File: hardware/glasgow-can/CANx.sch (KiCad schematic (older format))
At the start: 14 parts, among them J7 Conn_01x02_Male, Q1 TLP240A, Q2 NX7002BKW, U1 TCAN1051

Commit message: tidy up schematics
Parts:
- removed J7: Conn_01x02_Male, Connector_PinHeader_2.54mm:PinHeader_1x02_P2.54mm_Vertical, symbol Connector:Conn_01x02_Male
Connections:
- net CANH: now also D1.2 (A2); no longer D1.1 (A1)
- net CANL: now also D1.1 (A1); no longer D1.2 (A2)
- net S renamed SILENT
- no-connect marks 0 -> 1
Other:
- note added: "R1 is 1206 / 125mW\nIn fault (bus shorted) it will see:\nV= 24v R= 120Ω P= 24²/120= 4.8W"
- note added: "Red: Vf=2.0v Vr=3.0v I=100uA R=30kΩ\nGreen: Vf=3.0v Vr=2.0v I=20uA R=100kΩ *\nBlue: Vf=3.0v Vr=2.0v I=100uA R=20kΩ\n\n* Green has far higher lumosity, so current is reduced."
- note added: "Red:\nGreen:\nBlue:"
- note added: "Silent Active\nCAN Tx\nCAN Rx"
- note added: "Status LED"
- note added: "Termination"
- note added: "V= 5v I= 7.5mA\nVf= 1.27v Vr= 3.73v\nR= 506Ω -> 510Ω"
- note removed: "I=200mA R=120Ohm P=4.8W"
- note removed: "Red: Vf=2.0v I=100uA Vr=3.0v R=30kOhm\nGreen: Vf=3.0v I=20uA Vr=2.0v R=100kOhm\nBlue: Vf=3.0v I=100uA Vr=2.0v R=20kOhm"
- note removed: "V = 5v Vf = 1.27v \nVr = 3.73v I = 7.5mA\nR = 506 Ohm -> 510 Ohm"
- moved on the sheet: C1, C2, D1, D2, Q1, Q2, R1, R2, R3, R4, R5, R6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

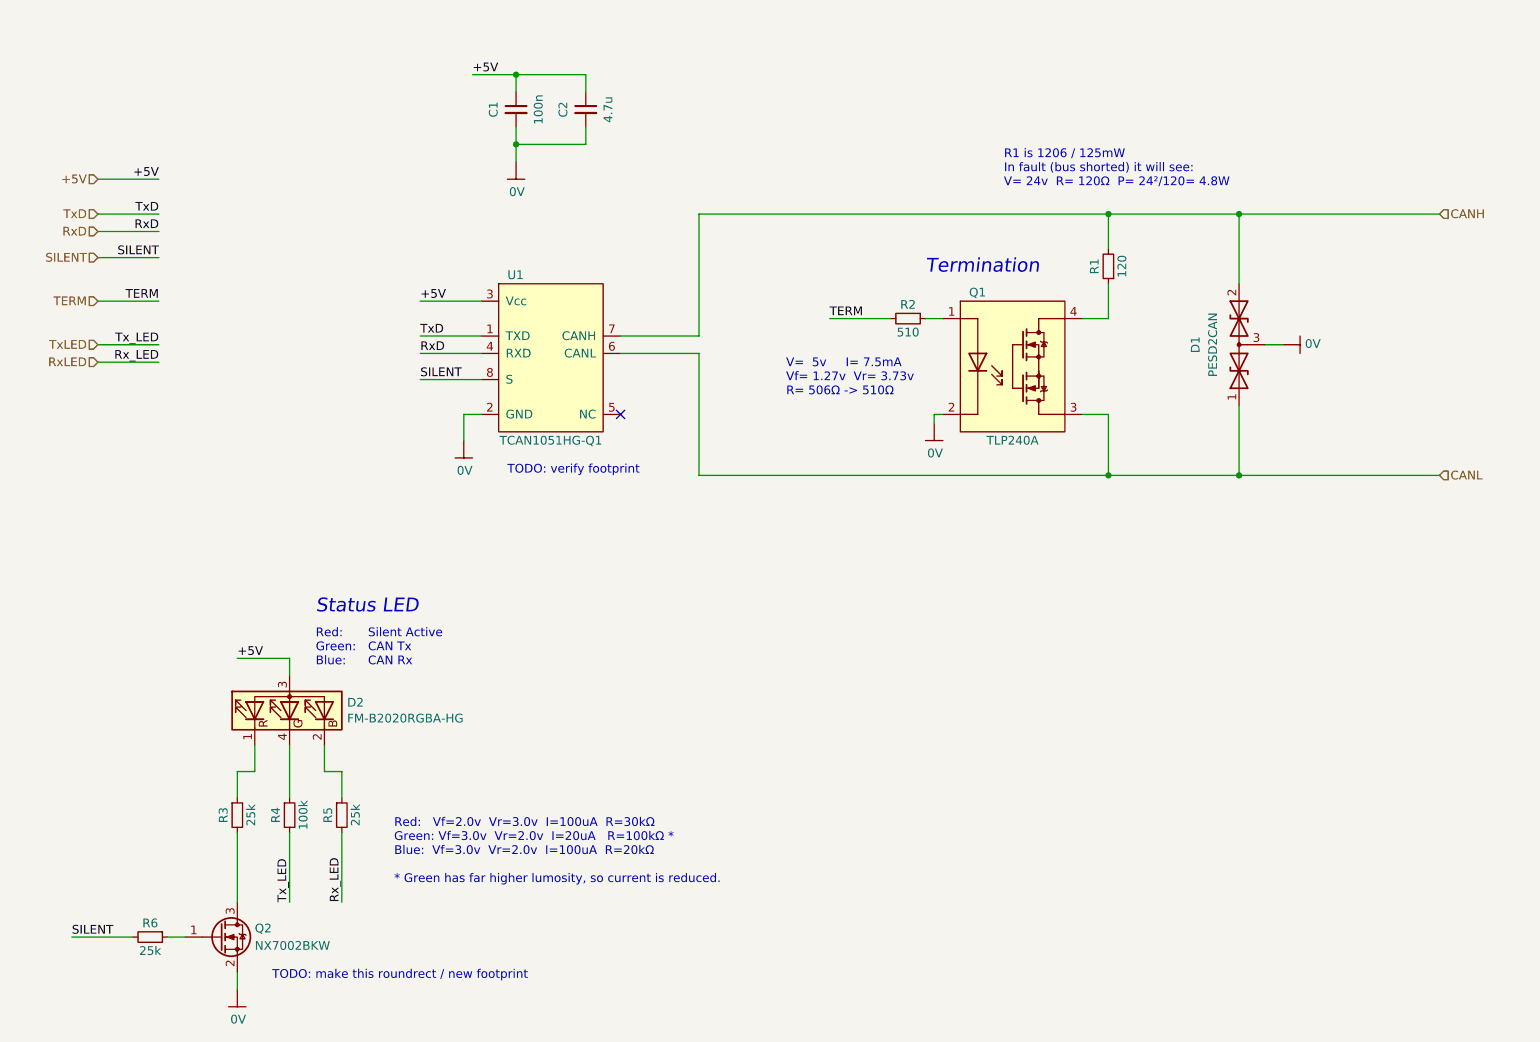
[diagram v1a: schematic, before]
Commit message: schematic revised according to discussion in #1, and layout mostly complete... some TODOs remain
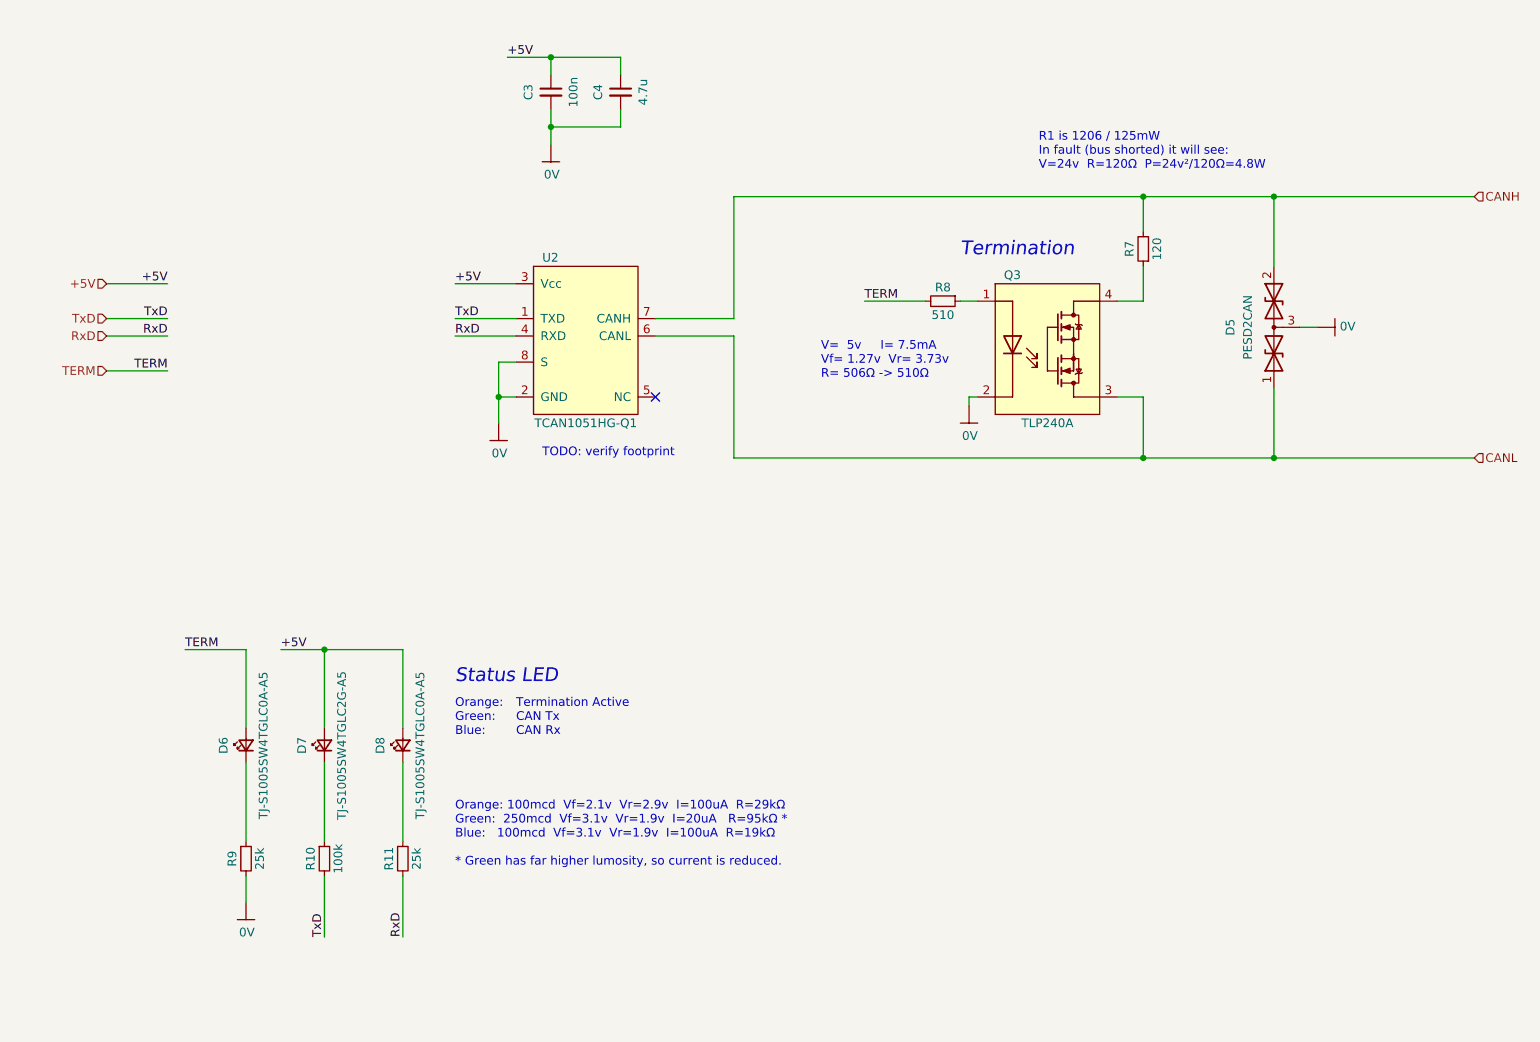
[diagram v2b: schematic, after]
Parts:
- removed D2: FM-B2020RGBA-HG, pkl_led:LED_TRI_2020, symbol Device:LED_RBAG
- removed Q2: NX7002BKW, Package_TO_SOT_SMD:SOT-323_SC-70, symbol Device:Q_NMOS_GSD
- removed R6: 25k, Resistor_SMD:R_0402_1005Metric, symbol Device:R_Small
- added D2, D4: TJ-S1005SW4TGLC0A-A5, LED_SMD:LED_0402_1005Metric_Pad0.77x0.64mm_HandSolder, symbol Device:LED_Small
- added D3: TJ-S1005SW4TGLC2G-A5, LED_SMD:LED_0402_1005Metric_Pad0.77x0.64mm_HandSolder, symbol Device:LED_Small
- Q1: MPN TLP240A -> TLP240A(TP1,F
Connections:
- net RxLED is gone; now on net RxD: R5.2
- net SILENT is gone; now on net 0V: U1.8 (S)
- net TxLED is gone; now on net TxD: R4.2
- net +5V: now also D3.2 (A), D4.2 (A)
- net 0V: now also R3.2
- net TERM: now also D2.2 (A)
- net at R4.1: now also D3.1 (K)
- net at R3.1: now also D2.1 (K)
- net at R5.1: now also D4.1 (K)
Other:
- note added: "Orange: 100mcd Vf=2.1v Vr=2.9v I=100uA R=29kΩ\nGreen: 250mcd Vf=3.1v Vr=1.9v I=20uA R=95kΩ *\nBlue: 100mcd Vf=3.1v Vr=1.9v I=100uA R=19kΩ\n\n* Green has far higher lumosity, so current is reduced."
- note added: "Orange:\nGreen:\nBlue:"
- note added: "R1 is 1206 / 125mW\nIn fault (bus shorted) it will see:\nV=24v R=120Ω P=24v²/120Ω=4.8W"
- note added: "Termination Active\nCAN Tx\nCAN Rx"
- note removed: "R1 is 1206 / 125mW\nIn fault (bus shorted) it will see:\nV= 24v R= 120Ω P= 24²/120= 4.8W"
- note removed: "Red: Vf=2.0v Vr=3.0v I=100uA R=30kΩ\nGreen: Vf=3.0v Vr=2.0v I=20uA R=100kΩ *\nBlue: Vf=3.0v Vr=2.0v I=100uA R=20kΩ\n\n* Green has far higher lumosity, so current is reduced."
- note removed: "Red:\nGreen:\nBlue:"
- note removed: "Silent Active\nCAN Tx\nCAN Rx"
- note removed: "TODO: make this roundrect / new footprint"
- moved on the sheet: C3, C4, D5, Q3, R7, R8, U2

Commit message: fix DE-9 footprint, spruce up schematic and layout
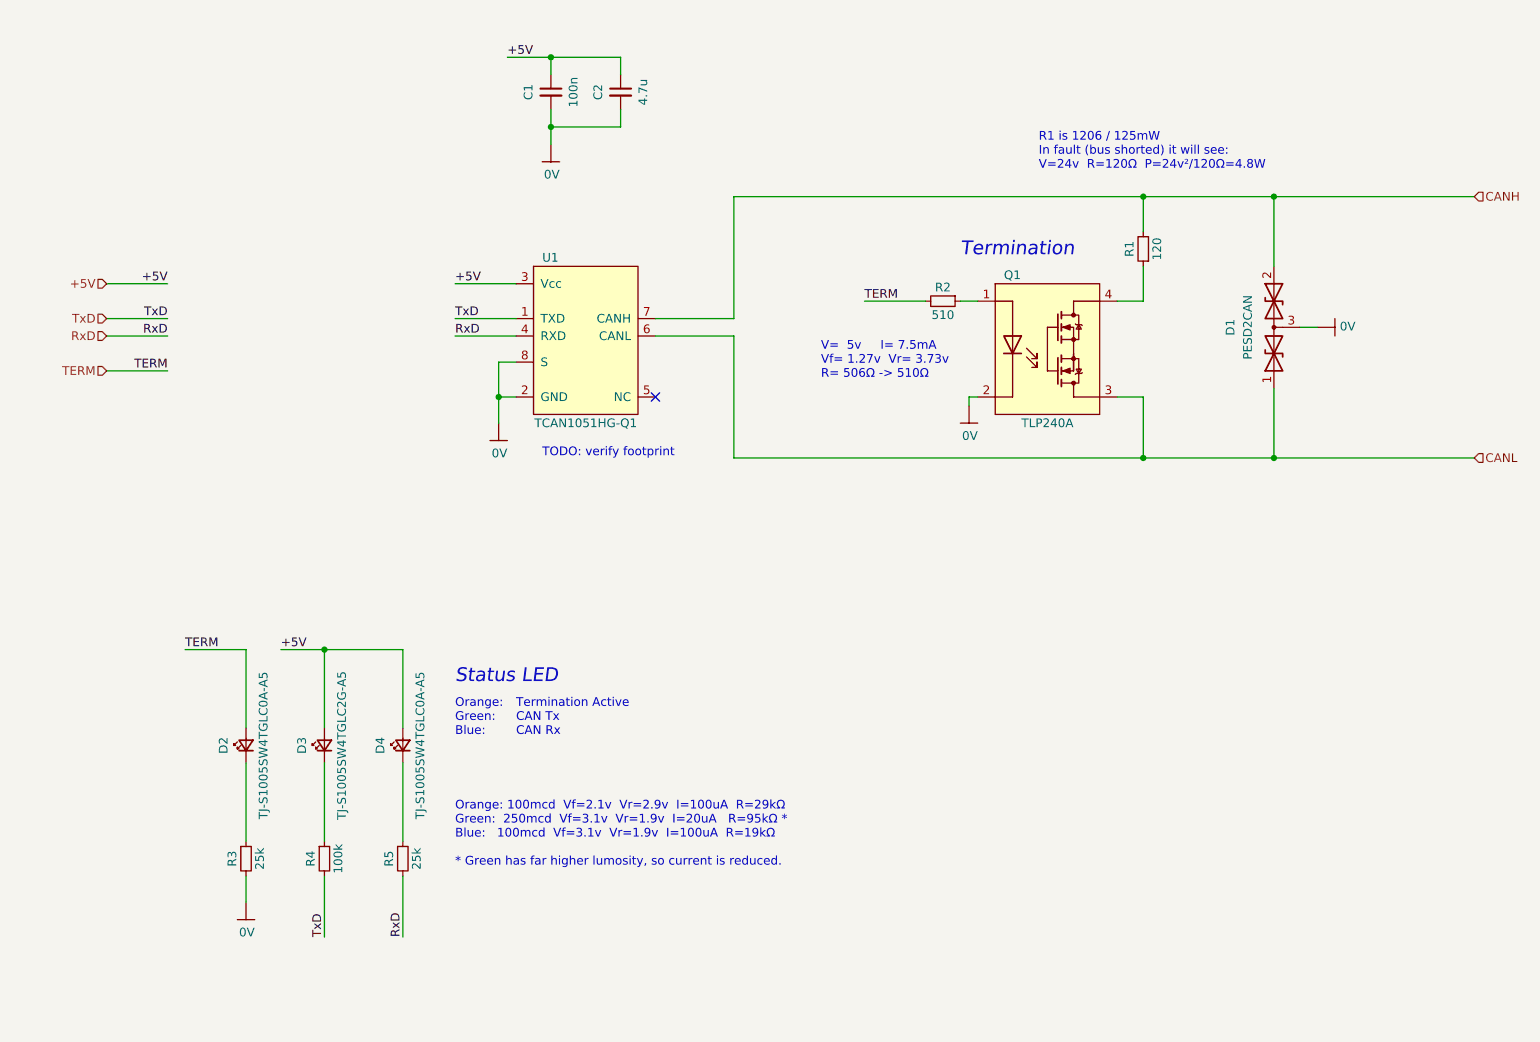
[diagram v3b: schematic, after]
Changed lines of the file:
@@
 $Descr A4 11693 8268
 encoding utf-8
-Sheet 3 3
+Sheet 2 3
 Title "Glasgow CAN Add-On"
 Date "2020-11-20"
@@
 AR Path="/5FCD3D33/5FBD7E1E" Ref="U?"  Part="1"
 AR Path="/5FD1E469/5FBD7E1E" Ref="U2"  Part="1"
-F 0 "U2" H 4400 3600 50  0000 L CNN
+F 0 "U1" H 4400 3600 50  0000 L CNN
 F 1 "TCAN1051" H 4650 3624 50  0001 C CNN
 F 2 "Package_DFN_QFN:DFN-8-1EP_3x3mm_P0.65mm_EP1.7x2.05mm" H 4400 2550 50  0001 L CNN
@@
 AR Path="/5FCD3D33/5FBD84AB" Ref="#PWR?"  Part="1"
 AR Path="/5FD1E469/5FBD84AB" Ref="#PWR014"  Part="1"
-F 0 "#PWR014" H 4150 3450 50  0001 C CNN
+F 0 "#PWR09" H 4150 3450 50  0001 C CNN
 F 1 "0V" H 4155 3477 50  0000 C CNN
 F 2 "" H 3850 3750 50  0001 C CNN
@@
 AR Path="/5FCD3D33/5FBE90CB" Ref="Q?"  Part="1"
 AR Path="/5FD1E469/5FBE90CB" Ref="Q3"  Part="1"
-F 0 "Q3" H 7050 3600 50  0000 L CNN
+F 0 "Q1" H 7050 3600 50  0000 L CNN
 F 1 "TLP240A" H 7300 2750 50  0000 C CNN
 F 2 "glasgow-can:TLP240A_5" H 7050 2650 50  0001 L CNN
@@
 AR Path="/5FCD3D33/5FBEAE62" Ref="#PWR?"  Part="1"
 AR Path="/5FD1E469/5FBEAE62" Ref="#PWR013"  Part="1"
-F 0 "#PWR013" H 6850 3350 50  0001 C CNN
+F 0 "#PWR08" H 6850 3350 50  0001 C CNN
 F 1 "0V" H 6855 3377 50  0000 C CNN
 F 2 "" H 6550 3650 50  0001 C CNN
@@
 AR Path="/5FCD3D33/5FBEBE4B" Ref="R?"  Part="1"
 AR Path="/5FD1E469/5FBEBE4B" Ref="R7"  Part="1"
-F 0 "R7" V 7900 2650 50  0000 C TNN
+F 0 "R1" V 7900 2650 50  0000 C TNN
 F 1 "120" V 7800 2650 50  0000 C BNN
 F 2 "Resistor_SMD:R_1206_3216Metric" H 7850 2650 50  0001 C CNN
@@
 AR Path="/5FCD3D33/5FBEA8CB" Ref="R?"  Part="1"
 AR Path="/5FD1E469/5FBEA8CB" Ref="R8"  Part="1"
-F 0 "R8" V 6650 2950 50  0000 C BNN
+F 0 "R2" V 6650 2950 50  0000 C BNN
 F 1 "510" V 6750 2950 50  0000 C TNN
 F 2 "Resistor_SMD:R_0402_1005Metric" H 6700 2950 50  0001 C CNN
@@
 AR Path="/5FCD3D33/5FBF5E92" Ref="D?"  Part="1"
 AR Path="/5FD1E469/5FBF5E92" Ref="D5"  Part="1"
-F 0 "D5" H 8600 3350 50  0000 C CNN
+F 0 "D1" H 8600 3350 50  0000 C CNN
 F 1 "PESD2CAN" H 8600 3250 50  0000 C CNN
 F 2 "rhais_package-smd:SOT-23" H 8450 3100 50  0001 C CNN
@@
 AR Path="/5FCD3D33/5FBF694A" Ref="#PWR?"  Part="1"
 AR Path="/5FD1E469/5FBF694A" Ref="#PWR012"  Part="1"
-F 0 "#PWR012" H 8850 2900 50  0001 C CNN
+F 0 "#PWR07" H 8850 2900 50  0001 C CNN
 F 1 "0V" V 8855 2972 50  0000 R CNN
 F 2 "" H 8550 3200 50  0001 C CNN
@@
 AR Path="/5FCD3D33/5FC20CDB" Ref="#PWR?"  Part="1"
 AR Path="/5FD1E469/5FC20CDB" Ref="#PWR011"  Part="1"
-F 0 "#PWR011" H 4450 1850 50  0001 C CNN
+F 0 "#PWR06" H 4450 1850 50  0001 C CNN
 F 1 "0V" H 4455 1877 50  0000 C CNN
 F 2 "" H 4150 2150 50  0001 C CNN
@@
 AR Path="/5FCD3D33/5FC25A3E" Ref="C?"  Part="1"
 AR Path="/5FD1E469/5FC25A3E" Ref="C4"  Part="1"
-F 0 "C4" V 4750 1750 50  0000 C BNN
+F 0 "C2" V 4750 1750 50  0000 C BNN
 F 1 "4.7u" V 4950 1750 50  0000 C TNN
 F 2 "Capacitor_SMD:C_0603_1608Metric" H 4850 1750 50  0001 C CNN
@@
 AR Path="/5FCD3D33/5FC25EC7" Ref="C?"  Part="1"
 AR Path="/5FD1E469/5FC25EC7" Ref="C3"  Part="1"
-F 0 "C3" V 4350 1750 50  0000 C BNN
+F 0 "C1" V 4350 1750 50  0000 C BNN
 F 1 "100n" V 4550 1750 50  0000 C TNN
 F 2 "Capacitor_SMD:C_0402_1005Metric" H 4450 1750 50  0001 C CNN
@@
 AR Path="/5FCD3D33/5FC08BB3" Ref="#PWR?"  Part="1"
 AR Path="/5FD1E469/5FC08BB3" Ref="#PWR015"  Part="1"
-F 0 "#PWR015" H 2700 6200 50  0001 C CNN
+F 0 "#PWR010" H 2700 6200 50  0001 C CNN
 F 1 "0V" H 2705 6227 50  0000 C CNN
 F 2 "" H 2400 6500 50  0001 C CNN
@@
 AR Path="/5FCD3D33/5FC897F6" Ref="D?"  Part="1"
 AR Path="/5FD1E469/5FC897F6" Ref="D6"  Part="1"
-F 0 "D6" H 2700 5600 50  0000 C BNN
+F 0 "D2" H 2700 5600 50  0000 C BNN
 F 1 "TJ-S1005SW4TGLC0A-A5" H 2700 5400 50  0000 C CNN
 F 2 "LED_SMD:LED_0402_1005Metric_Pad0.77x0.64mm_HandSolder" V 2700 5500 50  0001 C CNN
@@
 AR Path="/5FCD3D33/5FC8FDFC" Ref="R?"  Part="1"
 AR Path="/5FD1E469/5FC8FDFC" Ref="R11"  Part="1"
-F 0 "R11" V 3550 6150 50  0000 C BNN
+F 0 "R5" V 3550 6150 50  0000 C BNN
 F 1 "25k" V 3650 6150 50  0000 C TNN
 F 2 "Resistor_SMD:R_0402_1005Metric" H 3600 6150 50  0001 C CNN
@@
 AR Path="/5FCD3D33/5FC8FE04" Ref="R?"  Part="1"
 AR Path="/5FD1E469/5FC8FE04" Ref="R10"  Part="1"
-F 0 "R10" V 3100 6150 50  0000 C BNN
+F 0 "R4" V 3100 6150 50  0000 C BNN
 F 1 "100k" V 3200 6150 50  0000 C TNN
 F 2 "Resistor_SMD:R_0402_1005Metric" H 3150 6150 50  0001 C CNN
@@
 AR Path="/5FCD3D33/5FC94AD6" Ref="R?"  Part="1"
 AR Path="/5FD1E469/5FC94AD6" Ref="R9"  Part="1"
-F 0 "R9" V 2650 6150 50  0000 C BNN
+F 0 "R3" V 2650 6150 50  0000 C BNN
 F 1 "25k" V 2750 6150 50  0000 C TNN
 F 2 "Resistor_SMD:R_0402_1005Metric" H 2700 6150 50  0001 C CNN
@@
 AR Path="/5FCD3D33/5FCB8AEE" Ref="D?"  Part="1"
 AR Path="/5FD1E469/5FCB8AEE" Ref="D7"  Part="1"
-F 0 "D7" H 3150 5600 50  0000 C BNN
+F 0 "D3" H 3150 5600 50  0000 C BNN
 F 1 "TJ-S1005SW4TGLC2G-A5" H 3150 5400 50  0000 C CNN
 F 2 "LED_SMD:LED_0402_1005Metric_Pad0.77x0.64mm_HandSolder" V 3150 5500 50  0001 C CNN
@@
 AR Path="/5FCD3D33/5FCB8E6D" Ref="D?"  Part="1"
 AR Path="/5FD1E469/5FCB8E6D" Ref="D8"  Part="1"
-F 0 "D8" H 3600 5600 50  0000 C BNN
+F 0 "D4" H 3600 5600 50  0000 C BNN
 F 1 "TJ-S1005SW4TGLC0A-A5" H 3600 5400 50  0000 C CNN
 F 2 "LED_SMD:LED_0402_1005Metric_Pad0.77x0.64mm_HandSolder" V 3600 5500 50  0001 C CNN
